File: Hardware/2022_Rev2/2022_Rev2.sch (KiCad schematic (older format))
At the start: 14 parts

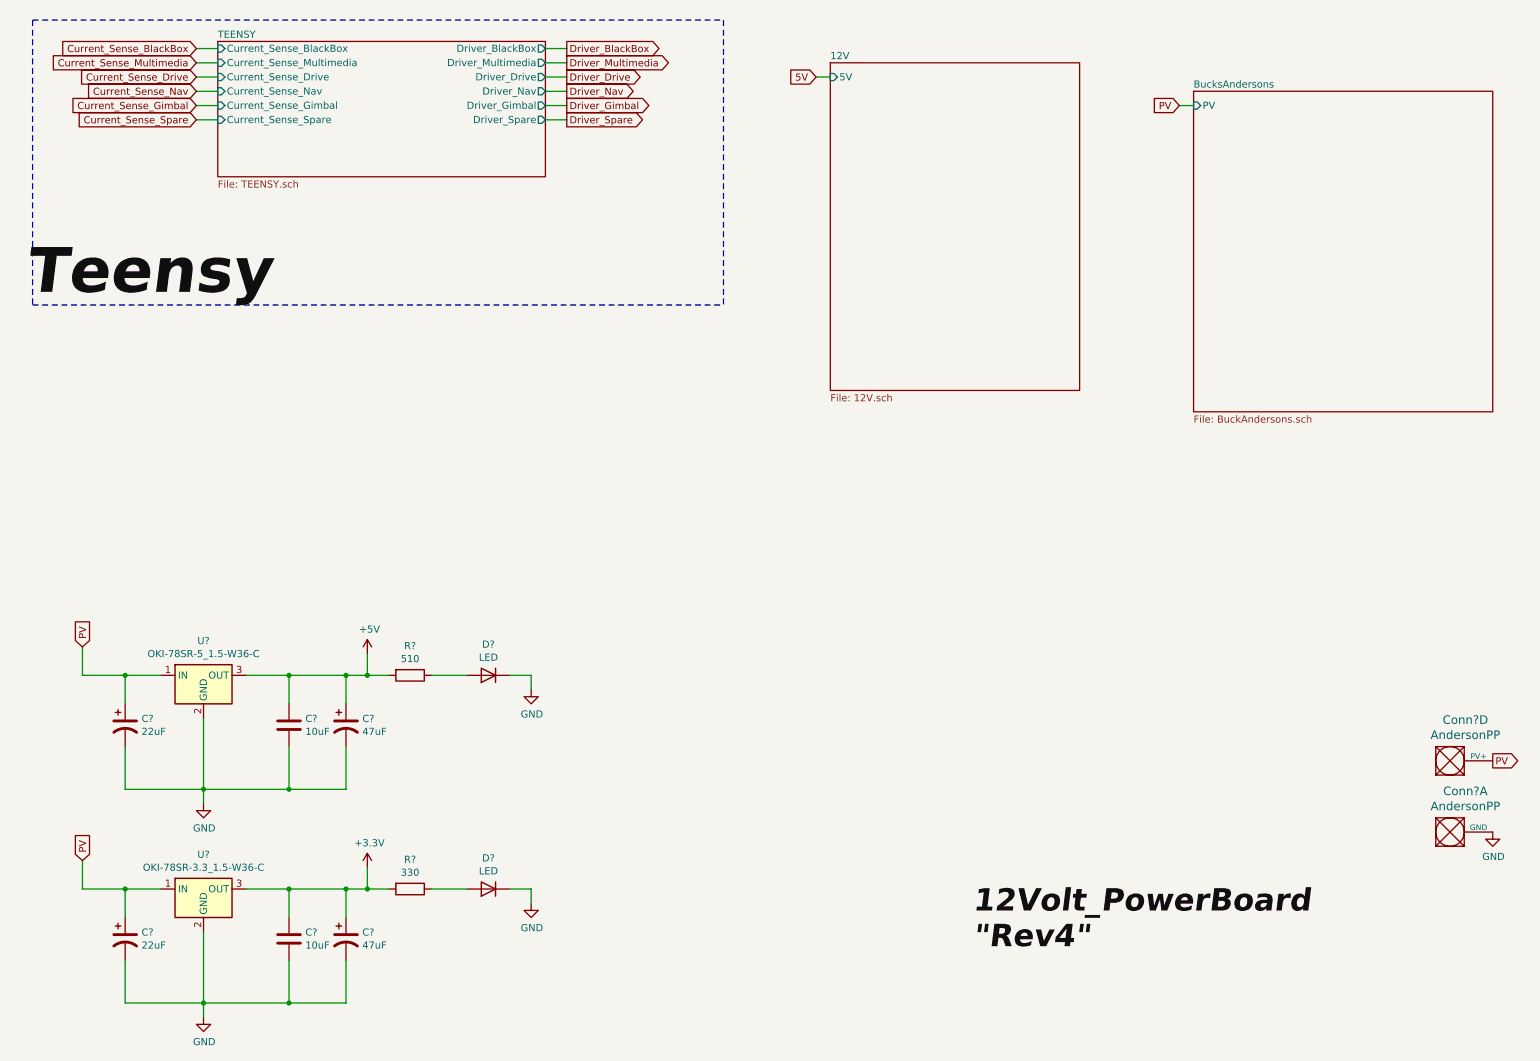
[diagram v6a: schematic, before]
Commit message: teensy pins are done (I think)
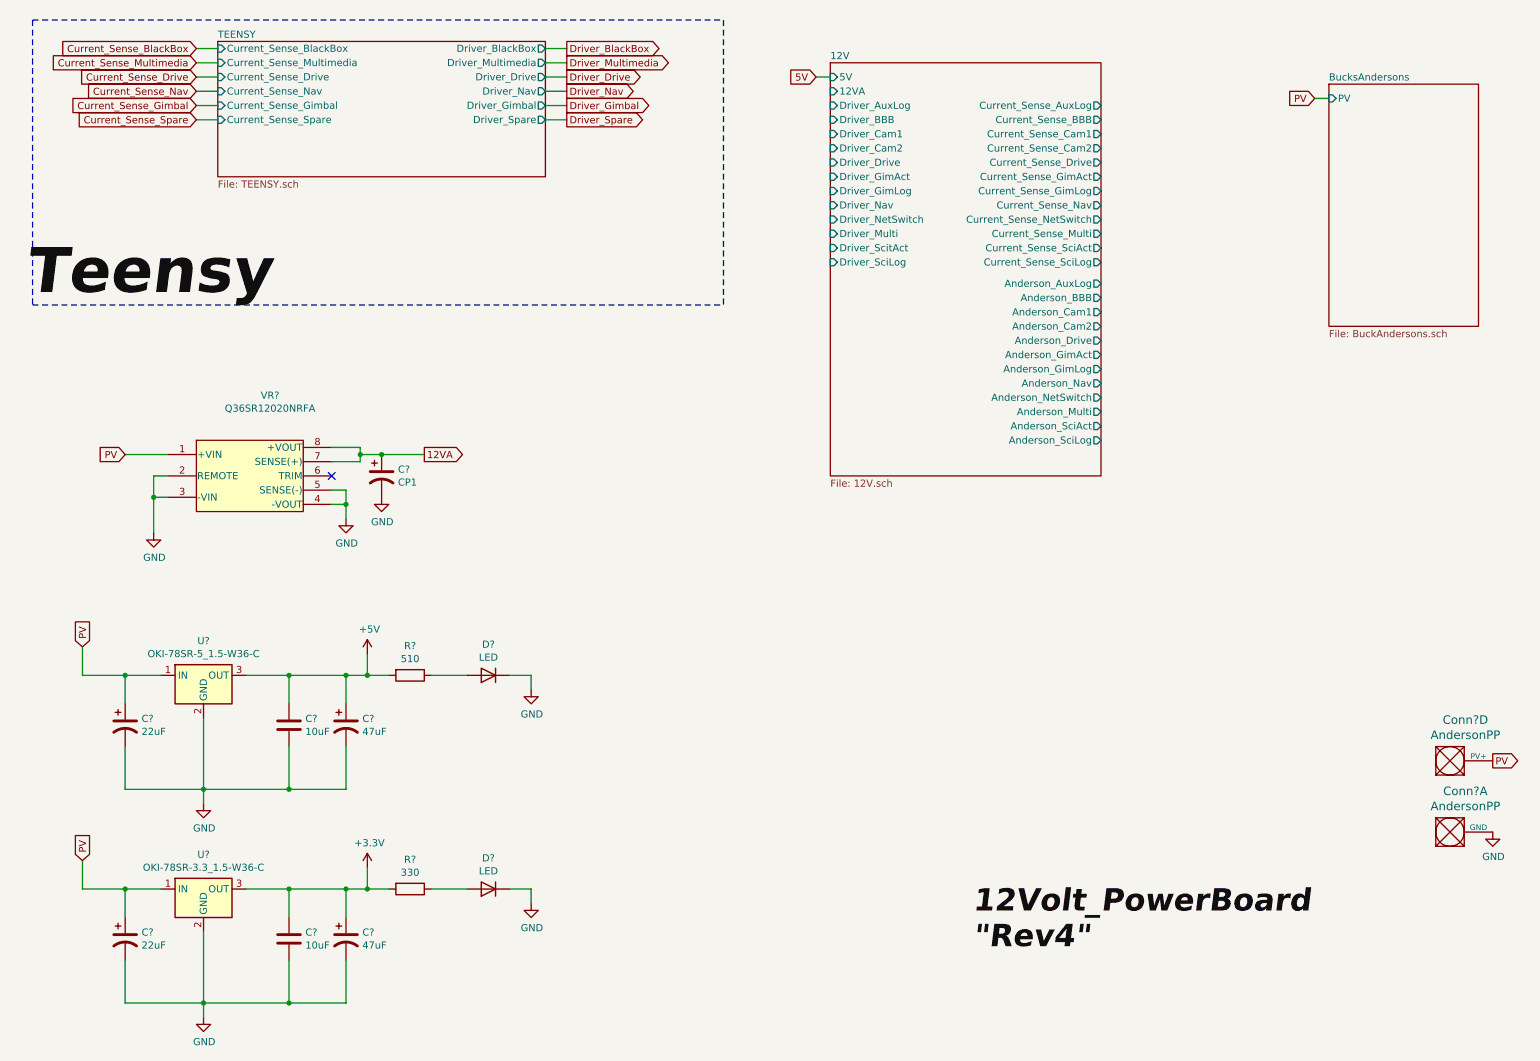
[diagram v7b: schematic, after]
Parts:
- added C?: CP1, symbol Device:CP1
- added VR?: Q36SR12020NRFA, symbol MRDT_Devices:Q36SR12020NRFA
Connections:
- net GND: now also C?.2, VR?.2 (REMOTE), VR?.3 (-VIN), VR?.4 (-VOUT), VR?.5 (SENSE(-))
- net PV: now also VR?.1 (+VIN)
- new net 12VA: C?.1, VR?.7 (SENSE(+)), VR?.8 (+VOUT)
- no-connect marks 0 -> 1
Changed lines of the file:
@@
 $Descr A4 11693 8268
 encoding utf-8
-Sheet 1 6
+Sheet 1 5
 Title ""
 Date ""
@@
 $EndDescr
 $Sheet
-S 6100 800  1750 2300
+S 6100 800  1900 2900
 U 62118E70
 F0 "12V" 50
 F1 "12V.sch" 50
 F2 "5V" I L 6100 900 50
+F3 "Driver_Drive" I L 6100 1500 50
+F4 "Driver_Nav" I L 6100 1800 50
+F5 "Current_Sense_Drive" O R 8000 1500 50
+F6 "Current_Sense_Nav" O R 8000 1800 50
+F7 "Anderson_Drive" O R 8000 2750 50
+F8 "Current_Sense_GimAct" O R 8000 1600 50
+F9 "Anderson_GimAct" O R 8000 2850 50
+F10 "Driver_GimAct" I L 6100 1600 50
+F11 "Current_Sense_SciAct" O R 8000 2100 50
+F12 "Anderson_SciAct" O R 8000 3350 50
+F13 "Driver_ScitAct" I L 6100 2100 50
+F14 "Current_Sense_Cam1" O R 8000 1300 50
+F15 "Current_Sense_Cam2" O R 8000 1400 50
+F16 "Current_Sense_GimLog" O R 8000 1700 50
+F17 "Current_Sense_Multi" O R 8000 2000 50
+F18 "Current_Sense_NetSwitch" O R 8000 1900 50
+F19 "Current_Sense_SciLog" O R 8000 2200 50
+F20 "Anderson_BBB" O R 8000 2450 50
+F21 "Anderson_Cam1" O R 8000 2550 50
+F22 "Anderson_Cam2" O R 8000 2650 50
+F23 "Anderson_GimLog" O R 8000 2950 50
+F24 "Anderson_Multi" O R 8000 3250 50
+F25 "Anderson_Nav" O R 8000 3050 50
+F26 "Anderson_NetSwitch" O R 8000 3150 50
+F27 "Anderson_SciLog" O R 8000 3450 50
+F28 "Driver_BBB" I L 6100 1200 50
+F29 "Driver_Cam1" I L 6100 1300 50
+F30 "Driver_Cam2" I L 6100 1400 50
+F31 "Driver_GimLog" I L 6100 1700 50
+F32 "Driver_Multi" I L 6100 2000 50
+F33 "Driver_NetSwitch" I L 6100 1900 50
+F34 "Driver_SciLog" I L 6100 2200 50
+F35 "12VA" I L 6100 1000 50
+F36 "Current_Sense_AuxLog" O R 8000 1100 50
+F37 "Current_Sense_BBB" O R 8000 1200 50
+F38 "Anderson_AuxLog" O R 8000 2350 50
+F39 "Driver_AuxLog" I L 6100 1100 50
 $EndSheet
 $Sheet
@@
 	1    0    0    -1
 $EndComp
-Text GLabel 8550 1100 0    50   Input ~ 0
+Text GLabel 9500 1050 0    50   Input ~ 0
 PV
 Wire Wire Line
-	8550 1100 8650 1100
+	9500 1050 9600 1050
 Text GLabel 6000 900  0    50   Input ~ 0
 5V
@@
 	6000 900  6100 900
 $Sheet
-S 8650 1000 2100 2250
+S 9600 950  1050 1700
 U 6217B740
 F0 "BucksAndersons" 50
 F1 "BuckAndersons.sch" 50
-F2 "PV" I L 8650 1100 50
+F2 "PV" I L 9600 1050 50
 $EndSheet
 $Comp
@@
 Text Label 7100 7050 0    157  Italic 31
 "Rev4"
+$Comp
+L MRDT_Devices:Q36SR12020NRFA VR?
+U 1 1 6246FE4F
+P 1650 3950
+F 0 "VR?" H 2167 4765 50  0000 C CNN
+F 1 "Q36SR12020NRFA" H 2167 4674 50  0000 C CNN
+F 2 "" H 1950 4750 50  0001 C CNN
+F 3 "" H 1950 4750 50  0001 C CNN
+	1    1650 3950
+	1    0    0    -1
+$EndComp
+Wire Wire Line
+	1450 3550 1150 3550
+Text GLabel 1150 3550 0    50   Input ~ 0
+PV
+Wire Wire Line
+	1450 3700 1350 3700
+Wire Wire Line
+	1350 3700 1350 3850
+Wire Wire Line
+	1450 3850 1350 3850
+Wire Wire Line
+	1350 3850 1350 4100
+Connection ~ 1350 3850
+$Comp
+L power:GND #PWR?
+U 1 1 62475957
+P 1350 4100
+F 0 "#PWR?" H 1350 3850 50  0001 C CNN
+F 1 "GND" H 1355 3927 50  0000 C CNN
+F 2 "" H 1350 4100 50  0001 C CNN
+F 3 "" H 1350 4100 50  0001 C CNN
+	1    1350 4100
+	1    0    0    -1
+$EndComp
+NoConn ~ 2600 3700
+Wire Wire Line
+	2600 3500 2800 3500
+Wire Wire Line
+	2600 3600 2800 3600
+Wire Wire Line
+	2800 3500 2800 3550
+Wire Wire Line
+	2800 3550 2950 3550
+Connection ~ 2800 3550
+Wire Wire Line
+	2800 3550 2800 3600
+$Comp
+L Device:CP1 C?
+U 1 1 6247B945
+P 2950 3700
+F 0 "C?" H 3065 3746 50  0000 L CNN
+F 1 "CP1" H 3065 3655 50  0000 L CNN
+F 2 "" H 2950 3700 50  0001 C CNN
+F 3 "~" H 2950 3700 50  0001 C CNN
+	1    2950 3700
+	1    0    0    -1
+$EndComp
+Wire Wire Line
+	2950 3550 3250 3550
+Connection ~ 2950 3550
+Text GLabel 3250 3550 2    50   Output ~ 0
+12VA
+Wire Wire Line
+	2600 3800 2700 3800
+Wire Wire Line
+	2600 3900 2700 3900
+Wire Wire Line
+	2700 3800 2700 3900
+Connection ~ 2700 3900
+Wire Wire Line
+	2700 3900 2700 4000
+$Comp
+L power:GND #PWR?
+U 1 1 62483B13
+P 2700 4000
+F 0 "#PWR?" H 2700 3750 50  0001 C CNN
+F 1 "GND" H 2705 3827 50  0000 C CNN
+F 2 "" H 2700 4000 50  0001 C CNN
+F 3 "" H 2700 4000 50  0001 C CNN
+	1    2700 4000
+	1    0    0    -1
+$EndComp
+$Comp
+L power:GND #PWR?
+U 1 1 624844CA
+P 2950 3850
+F 0 "#PWR?" H 2950 3600 50  0001 C CNN
+F 1 "GND" H 2955 3677 50  0000 C CNN
+F 2 "" H 2950 3850 50  0001 C CNN
+F 3 "" H 2950 3850 50  0001 C CNN
+	1    2950 3850
+	1    0    0    -1
+$EndComp
 $EndSCHEMATC

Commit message: andersons done
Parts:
- removed C?: CP1, symbol Device:CP1
- removed VR?: Q36SR12020NRFA, symbol MRDT_Devices:Q36SR12020NRFA
- added Conn? (x22): AndersonPP, symbol MRDT_Connectors:AndersonPP
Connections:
- net labels added: Anderson_AuxLog, Anderson_BBB, Anderson_Cam1, Anderson_Cam2, Anderson_Drive, Anderson_GimAct, Anderson_GimLog, Anderson_Multi, Anderson_Nav, Anderson_NetSwitch, Anderson_SciAct, Anderson_SciLog, Current_Sense_AuxLog, Current_Sense_BBB, Current_Sense_Cam1, Current_Sense_Cam2, Current_Sense_GimAct, Current_Sense_GimLog, Current_Sense_Multi, Current_Sense_NetSwitch, Current_Sense_SciAct, Current_Sense_SciLog, Driver_AuxLog, Driver_BBB, Driver_Cam1, Driver_Cam2, Driver_GimAct, Driver_GimLog, Driver_Multi, Driver_NetSwitch, Driver_SciAct, Driver_SciLog
- net labels removed: 12VA, Current_Sense_BlackBox, Current_Sense_Gimbal, Current_Sense_Multimedia, Current_Sense_Spare, Driver_BlackBox, Driver_Gimbal, Driver_Multimedia, Driver_Spare
- wire segments 73 -> 158
- no-connect marks 1 -> 0
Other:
- moved on the sheet: Conn?A, Conn?D
